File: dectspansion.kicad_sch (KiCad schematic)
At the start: 24 parts, among them J1 Hexpansion-Connector, J2 Conn_01x03_Pin, J3 AudioJack4, J4 Conn_01x02_Pin, U1 SC14CVMDECT

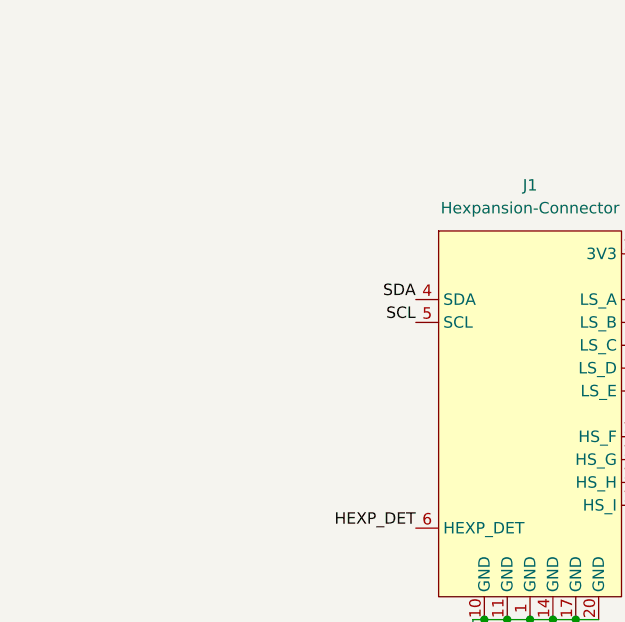
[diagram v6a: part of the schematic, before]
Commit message: Added eeprom to board, updated to prototype 2
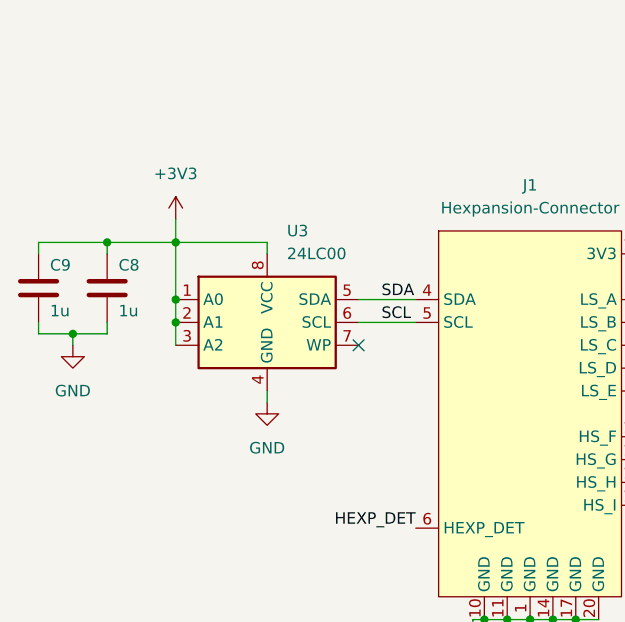
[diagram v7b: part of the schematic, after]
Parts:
- added C8, C9: 1u, Capacitor_SMD:C_0402_1005Metric, symbol Device:C
- added U3: 24LC00, Package_SO:TSSOP-8_4.4x3mm_P0.65mm, symbol Memory_EEPROM:24LC00
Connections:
- net +3V3: now also C8.1, C9.1, U3.1 (A0), U3.2 (A1), U3.3 (A2), U3.8 (VCC)
- net GND: now also C8.2, C9.2, U3.4 (GND)
- net SCL: now also U3.6 (SCL)
- net SDA: now also U3.5 (SDA)
- no-connect marks 10 -> 11

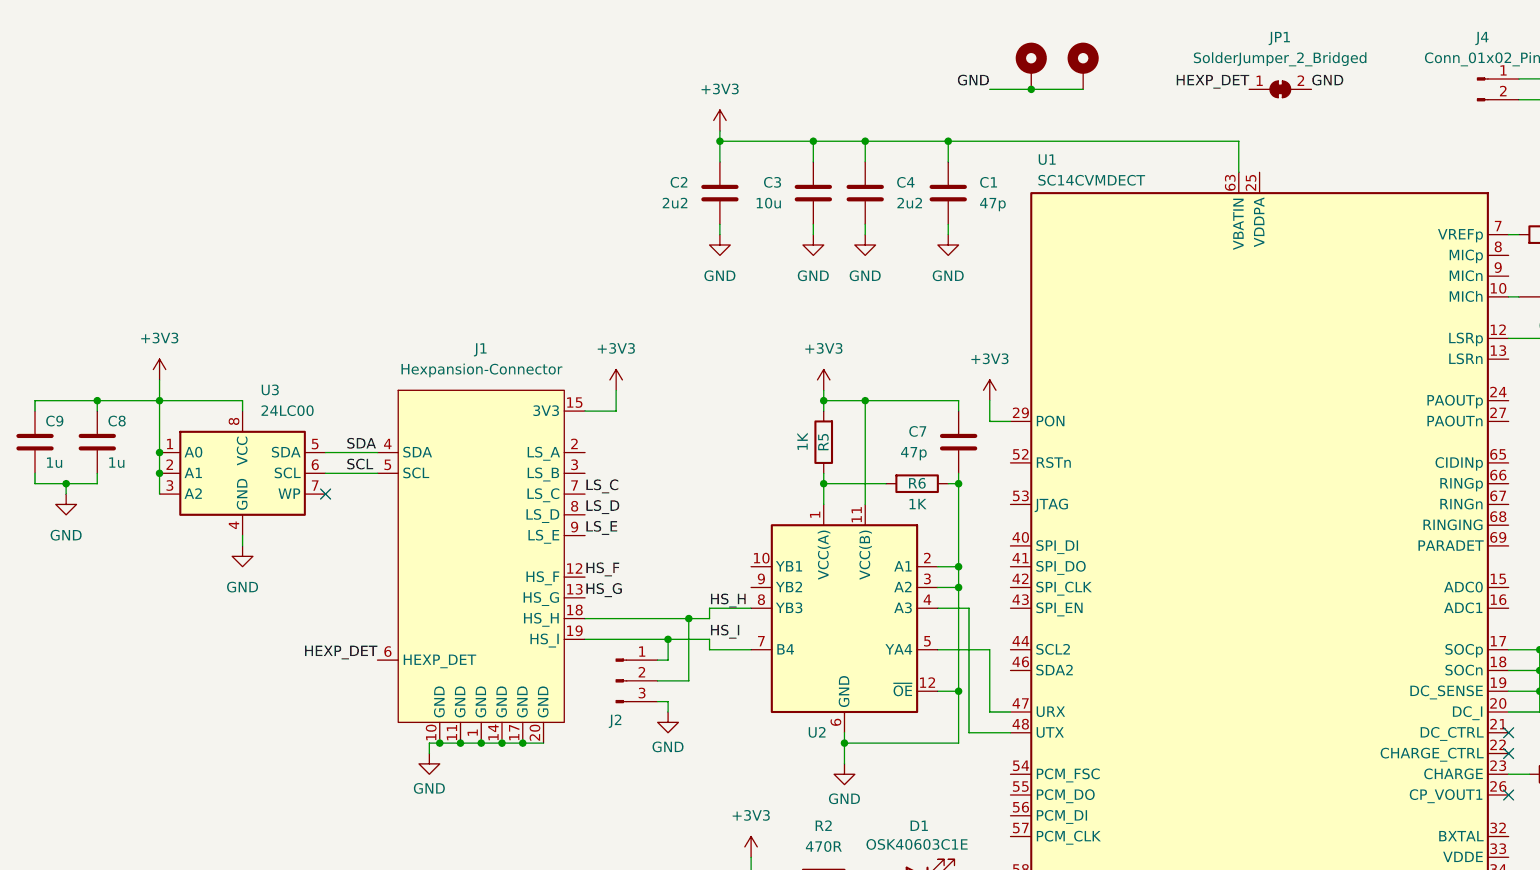
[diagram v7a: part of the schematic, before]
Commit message: Removed eeprom capacitors, and solder jumper
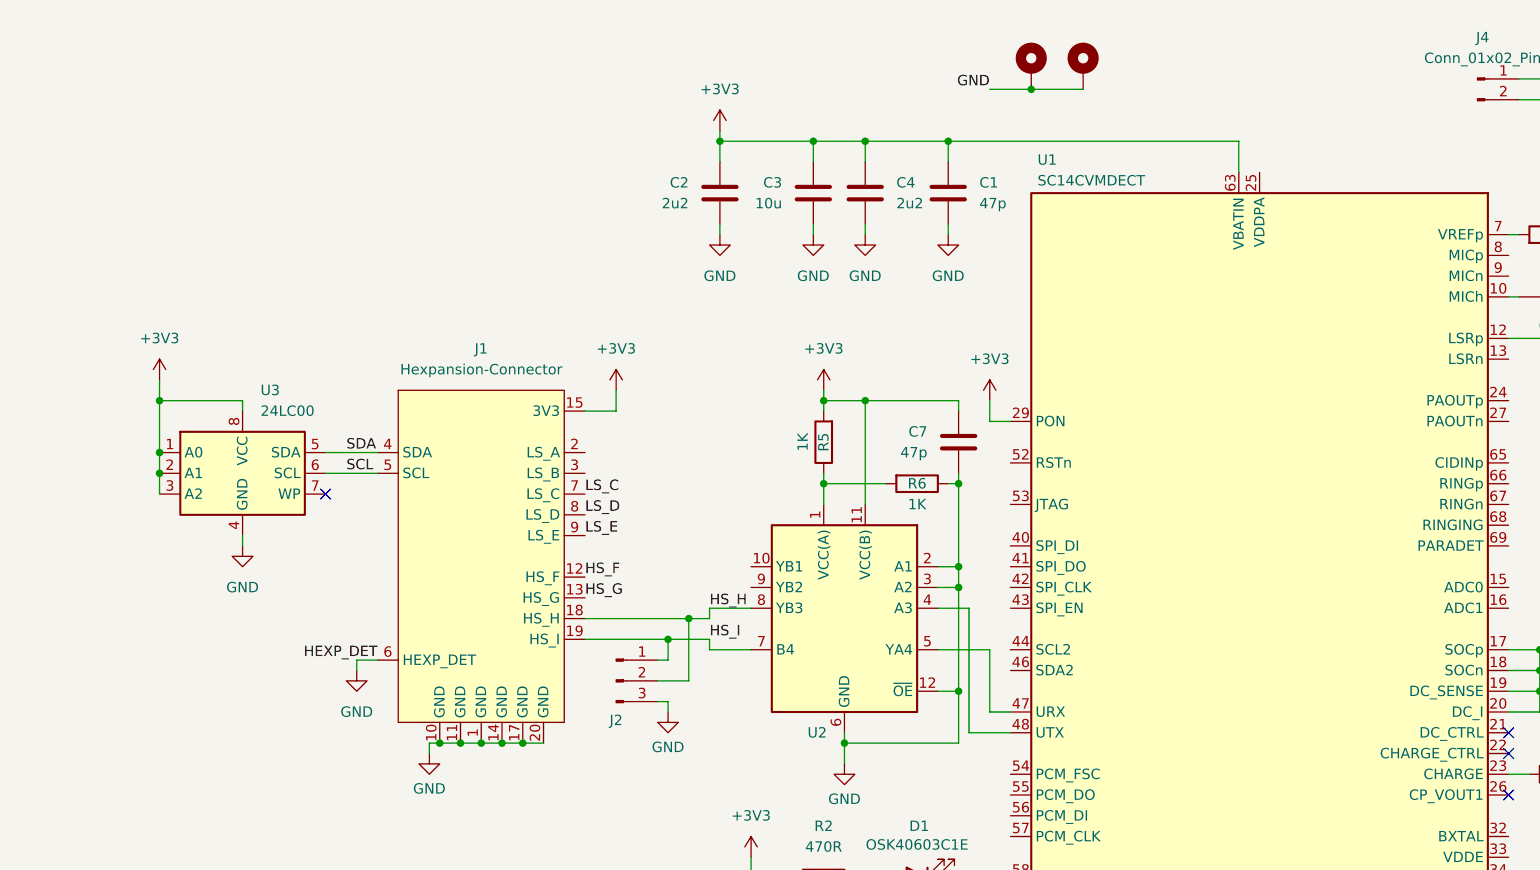
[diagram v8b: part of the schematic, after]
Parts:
- removed C8, C9: 1u, Capacitor_SMD:C_0402_1005Metric, symbol Device:C
- removed JP1: SolderJumper_2_Bridged, Jumper:SolderJumper-2_P1.3mm_Bridged_RoundedPad1.0x1.5mm, symbol Jumper:SolderJumper_2_Bridged
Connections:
- net HEXP_DET is gone; now on net GND: J1.6 (HEXP_DET)
